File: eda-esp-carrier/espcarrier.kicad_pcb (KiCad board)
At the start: 2 copper layers, 38.5 x 38.5 mm, 22 parts, among them J1 BATT, J3 DEBUG, Q1 PMF170XP, Q2 DMN2310U, SW1 PWR, SW2 RST, SW3 PRGM, U1 TP4056_board, U2 ESP-12E, U3 TLV75533PDBV

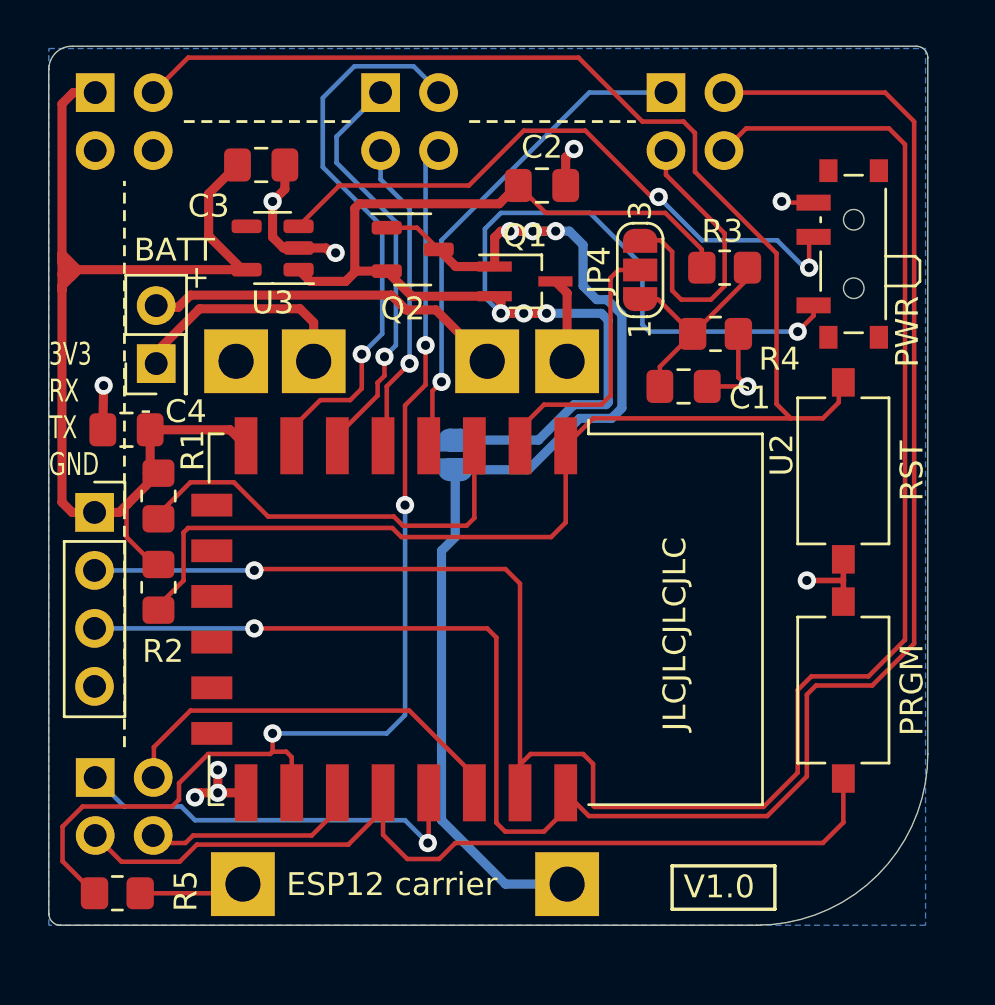
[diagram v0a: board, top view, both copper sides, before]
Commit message: move some component
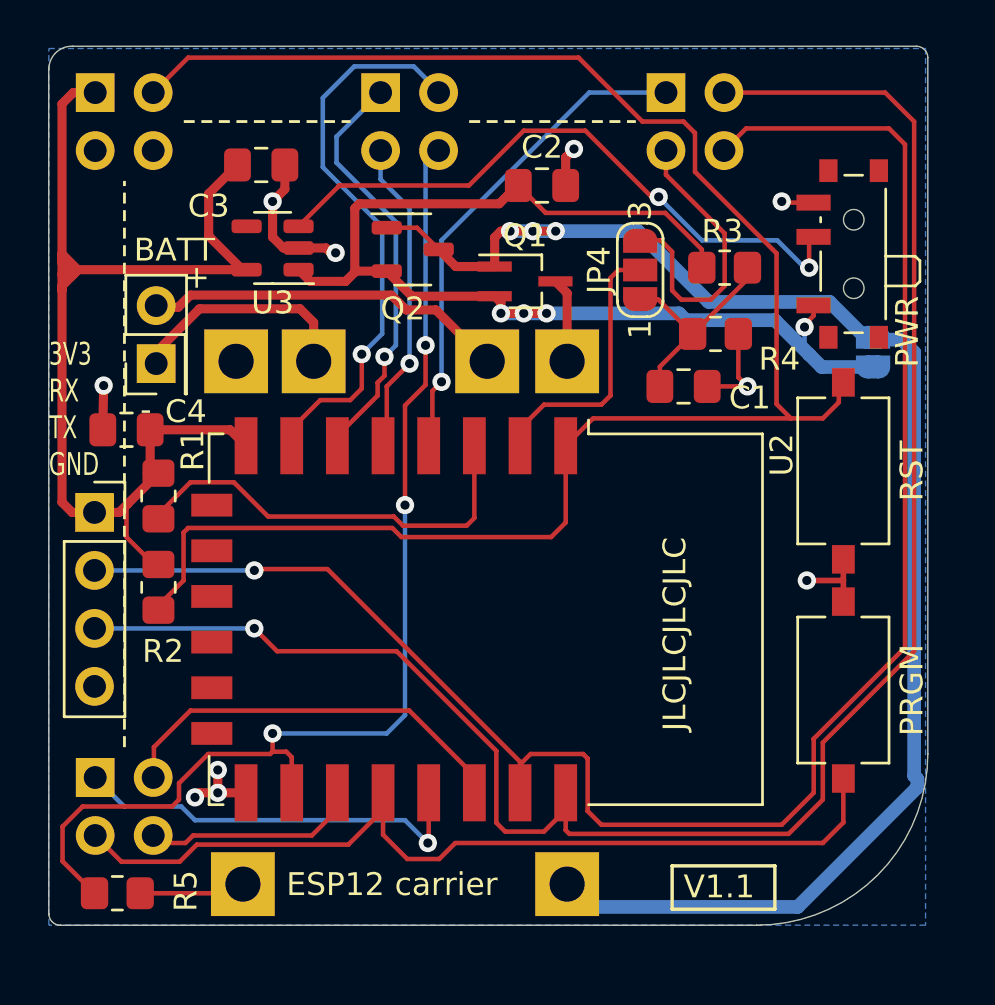
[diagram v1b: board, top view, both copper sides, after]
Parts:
- moved JP3 18.8 mm to (91.6, 116.1), turned to -90 degrees
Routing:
- net /VIN: track 71.0 -> 53.7 mm
- net Net-(JP3-A): track 51.7 -> 68.4 mm
- net RXD: track 83.9 -> 79.7 mm
- net TXD: track 82.9 -> 81.1 mm
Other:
- board text added: "V1.1"
- board text removed: "V1.0"

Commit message: work on RF rework
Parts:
- moved SW1 33.3 mm to (71.2, 139.0), turned to 0 degrees
- moved SW2 27.5 mm to (65.4, 132.9), turned to -90 degrees
- moved SW3 26.1 mm to (65.4, 123.2), turned to -90 degrees
- moved U2 6.28 mm to (80.9, 127.4)
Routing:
- net TXD: track 81.1 -> 0.00 mm, vias 1 -> 0
- net RXD: track 79.7 -> 0.00 mm, vias 1 -> 0
- net ~{RST}: track 78.2 -> 0.00 mm
- net Net-(JP3-A): track 68.4 -> 0.00 mm, vias 3 -> 0
- net /VIN: track 53.7 -> 0.00 mm, vias 4 -> 0
- net +3V3: track 51.5 -> 0.00 mm
- net GPIO15: track 49.2 -> 0.00 mm, vias 3 -> 0
- net GPIO0: track 39.8 -> 0.00 mm
- net EN: track 28.0 -> 0.00 mm, vias 2 -> 0
- net GND: track 27.2 -> 0.00 mm, vias 10 -> 0
- net GPIO13: track 24.9 -> 0.00 mm, vias 1 -> 0
- net GPIO16: track 21.7 -> 0.00 mm, vias 1 -> 0
- net Net-(U2-EN): track 18.8 -> 0.00 mm
- net GPIO12: track 18.4 -> 0.00 mm, vias 1 -> 0
- net GPIO4: track 18.0 -> 0.00 mm, vias 1 -> 0
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
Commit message: finish rf friendlier desgin
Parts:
- moved JP3 29.3 mm to (67.1, 132.2), turned to 90 degrees
- moved SW1 28.1 mm to (59.1, 113.7), turned to -90 degrees
- moved J1 15.9 mm to (75.6, 112.5), turned to 0 degrees
- moved R5 13.6 mm to (71.9, 137.6), turned to 180 degrees
- moved C4 13.4 mm to (71.8, 116.0), turned to -90 degrees
- moved SW2 9.61 mm to (64.9, 123.3), turned to 90 degrees
- moved SW3 9.61 mm to (64.9, 132.8), turned to 90 degrees
- moved C3 5.84 mm to (66.1, 113.6), turned to 180 degrees
- moved Q1 4.50 mm to (77.7, 108.7)
- moved C2 3.22 mm to (78.7, 106.0)
- moved C1 3.02 mm to (85.0, 115.1)
- moved R4 2.42 mm to (85.0, 112.9)
- moved R3 1.50 mm to (85.0, 110.9)
- moved U3 1.29 mm to (65.4, 110.2)
- moved U2 0.50 mm to (81.4, 127.4)
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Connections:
- net /VIN renamed VIN
- net Net-(J1-Pin_1) renamed /B-
- net Net-(J1-Pin_2) renamed /B+
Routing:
- net Net-(JP3-A): track 0.00 -> 73.0 mm, vias 0 -> 3
- net TXD: track 0.00 -> 71.2 mm, vias 0 -> 1
- net VIN: track 0.00 -> 68.5 mm, vias 0 -> 4
- net ~{RST}: track 0.00 -> 66.0 mm
- net RXD: track 0.00 -> 59.5 mm, vias 0 -> 1
- net +3V3: track 0.00 -> 50.9 mm, vias 0 -> 3
- net GPIO15: track 0.00 -> 44.7 mm, vias 0 -> 1
- net GPIO14: track 0.00 -> 41.9 mm, vias 0 -> 1
- net GPIO12: track 0.00 -> 38.6 mm, vias 0 -> 1
- net Net-(U2-EN): track 0.00 -> 36.3 mm
- net GPIO13: track 0.00 -> 35.4 mm, vias 0 -> 1
- net GPIO4: track 0.00 -> 25.2 mm
- net GPIO5: track 0.00 -> 24.7 mm
- net GPIO0: track 0.00 -> 24.6 mm
- net GPIO16: track 0.00 -> 24.6 mm, vias 0 -> 1
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- added copper zone on F.Cu, net GND
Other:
- outline, holes or cut-outs redrawn
- board text added: "+ RX TX GND"
- board text added: "ESP12-carrier (c) 2024 Andreas Philipp"
- board text added: "V${REVISION}"
- board text added: "https://gitlab.com/ anphi/esp12-battery -breakout"
- board text removed: "3V3 RX TX GND"
- board text removed: "ESP12 carrier"
- board text removed: "ESP12 carrier board https://gitlab.com/anphi/ esp12-battery-breakout (c) 2024 - Andreas Philipp"
- board text removed: "V1.1"
